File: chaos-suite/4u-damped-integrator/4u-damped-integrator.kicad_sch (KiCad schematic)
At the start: 60 parts, among them J1 BananaJack_PanelMount, J10 BananaJack_PanelMount, J11 BananaJack_PanelMount, J12 I2_IO_Ctrl, J13 I2_IO_Main, J14 I2_Damping_Ctrl, J15 I2_Damping_Main, J16 BananaJack_PanelMount, J2 BananaJack_PanelMount, J3 BananaJack_PanelMount, J4 I1_IO_Ctrl, J5 I1_IO_Main, J6 I1_Damping_Ctrl, J7 I1_Damping_Main, J8 BananaJack_PanelMount, J9 BananaJack_PanelMount, Q1 2N3904, Q2 2N3906, Q3 2N3904, Q4 2N3906, U1 TL074, U2 LM13700

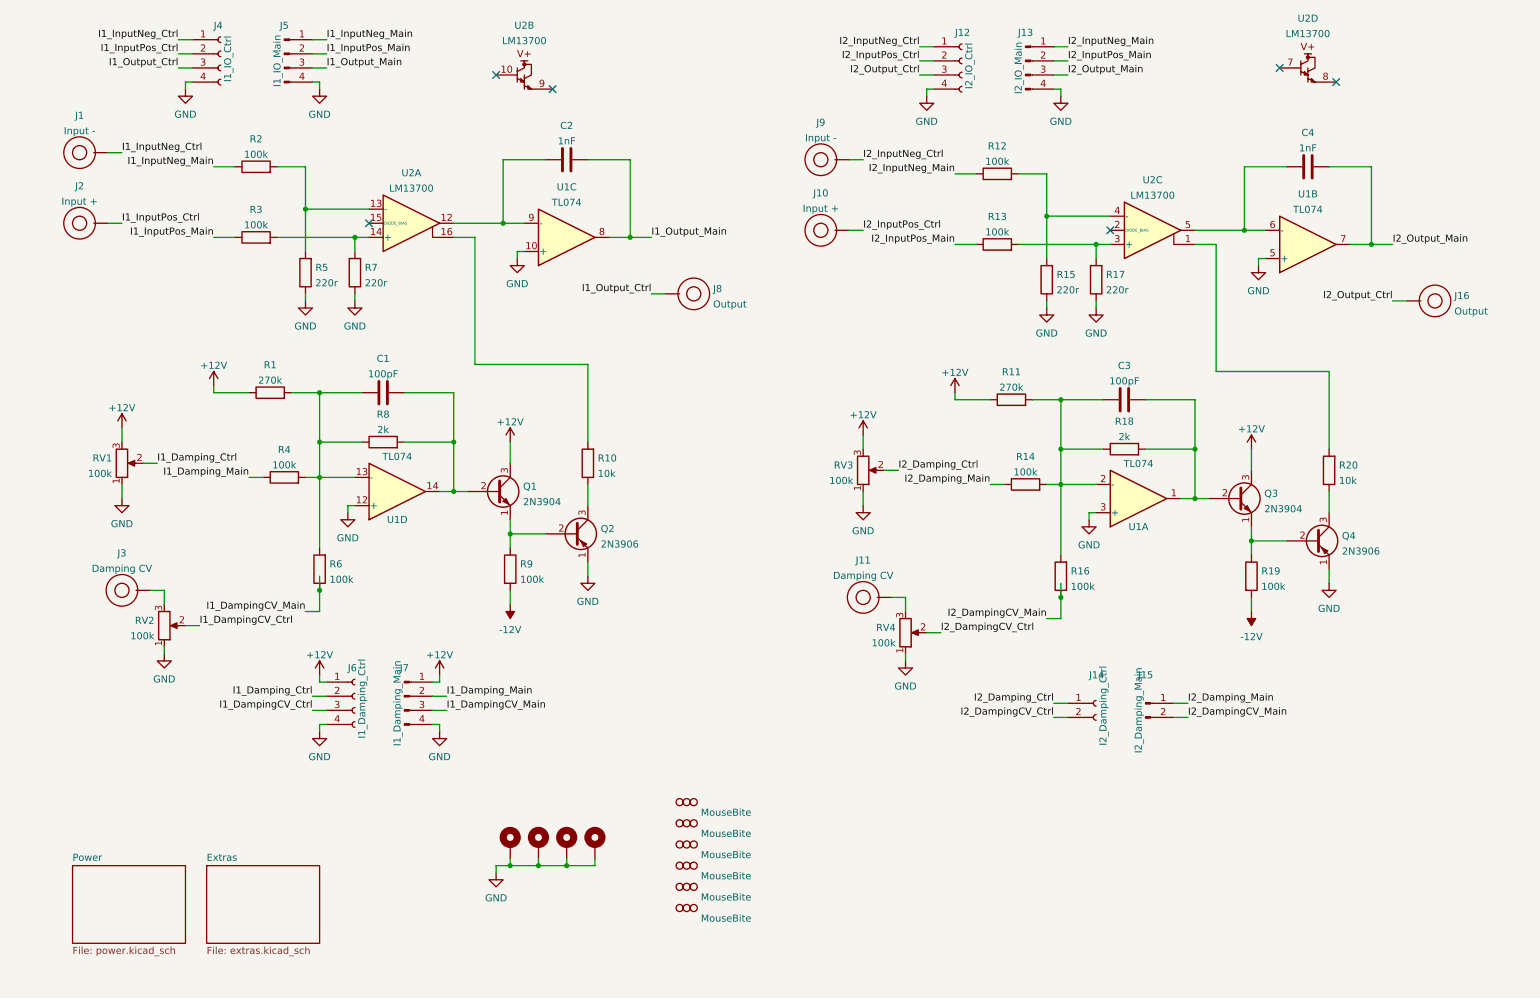
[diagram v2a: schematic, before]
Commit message: Updating damped integrator circuit and layout
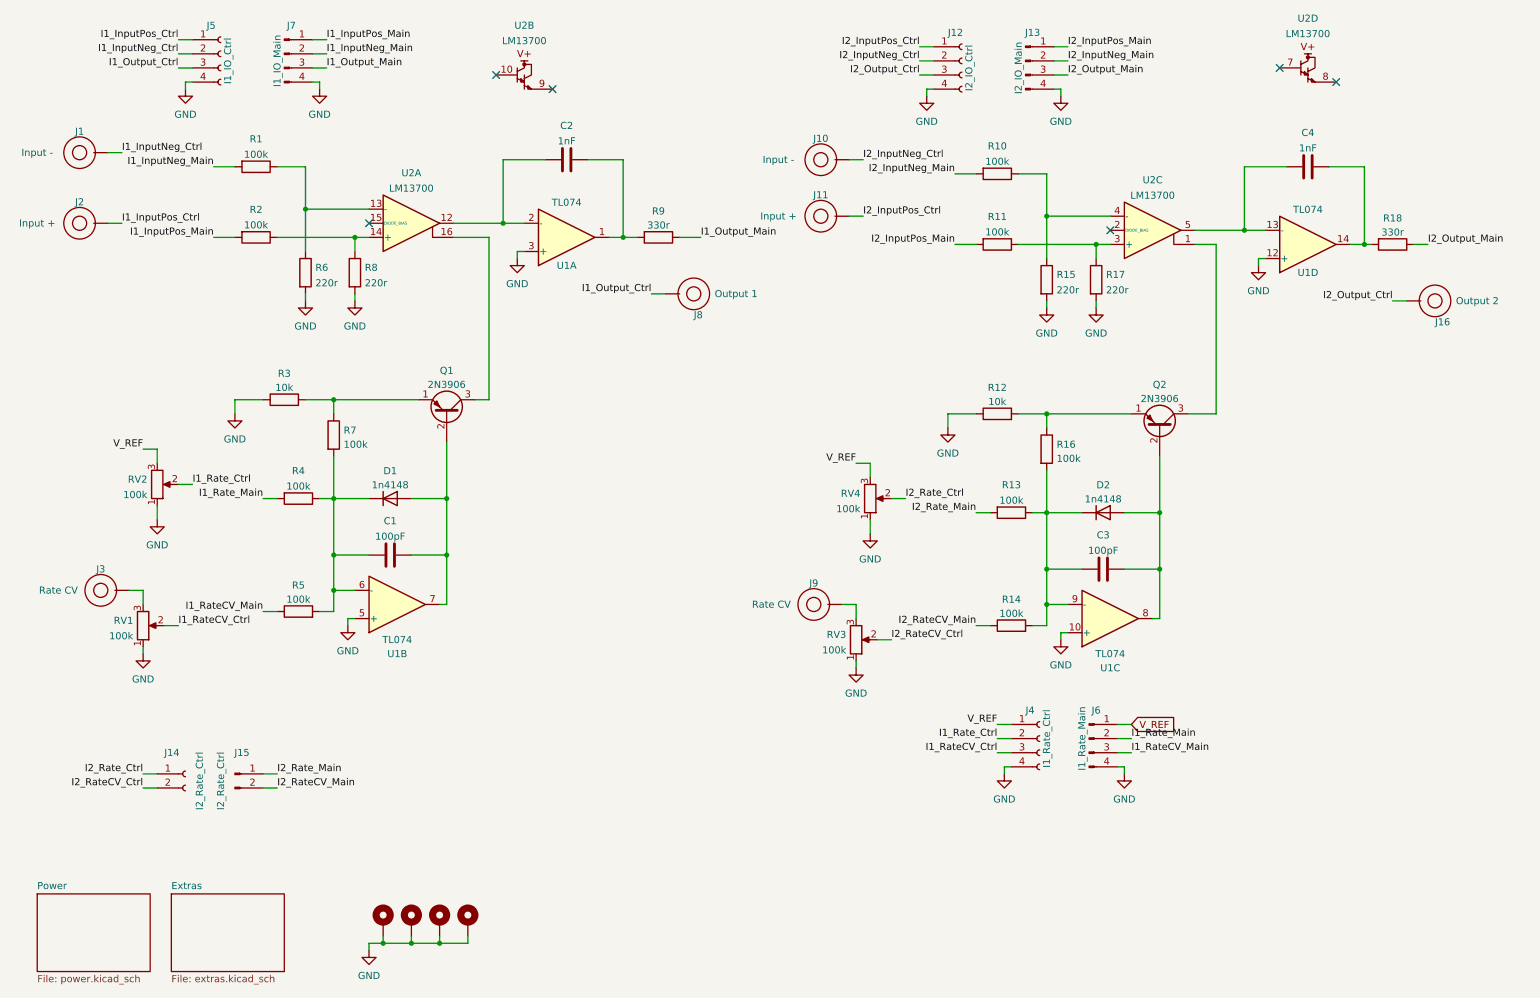
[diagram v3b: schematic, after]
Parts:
- removed H10, H5, H6, H7, H8, H9: MouseBite, Panelization:mouse-bite-2mm-slot, symbol Panelization:MouseBite
- removed J11: BananaJack_PanelMount, Rumblesan_Footprints:BananaJack_THT_JohnsonCinch_108-09, symbol BananaJacks:BananaJack_PanelMount
- removed Q1, Q3: 2N3904, Package_TO_SOT_THT:TO-92_Inline_Wide, symbol Transistor_BJT:2N3904
- removed Q4: 2N3906, Package_TO_SOT_THT:TO-92_Inline_Wide, symbol Transistor_BJT:2N3906
- removed R1, R11: 270k, Rumblesan_Footprints:Resistor_THT_L6.3mm_D2.5mm_P10.16mm_Horizontal, symbol Device:R
- removed R14, R16, R19, R9: 100k, Rumblesan_Footprints:Resistor_THT_L6.3mm_D2.5mm_P10.16mm_Horizontal, symbol Device:R
- removed R18, R8: 2k, Rumblesan_Footprints:Resistor_THT_L6.3mm_D2.5mm_P10.16mm_Horizontal, symbol Device:R
- removed R20: 10k, Rumblesan_Footprints:Resistor_THT_L6.3mm_D2.5mm_P10.16mm_Horizontal, symbol Device:R
- added D1, D2: 1n4148, rumblesan-standard-parts:D_DO-35_SOD27_P7.62mm_Horizontal, symbol Device:D
- added J9: Banana Socket PanelMount, rumblesan-standard-parts:BananaJack_THT_JohnsonCinch_108-09, symbol BananaJacks:Banana Socket PanelMount
- added Q2: 2N3906, Package_TO_SOT_THT:TO-92_Inline_Wide, symbol Transistor_BJT:2N3906
- added R12, R3: 10k, rumblesan-standard-parts:R_Axial_DIN0207_L6.3mm_D2.5mm_P10.16mm_Horizontal, symbol rumblesan-standard-parts:R
- added R13, R14, R16: 100k, rumblesan-standard-parts:R_Axial_DIN0207_L6.3mm_D2.5mm_P10.16mm_Horizontal, symbol rumblesan-standard-parts:R
- added R18, R9: 330r, rumblesan-standard-parts:R_Axial_DIN0207_L6.3mm_D2.5mm_P10.16mm_Horizontal, symbol rumblesan-standard-parts:R
- C1, C2, C3, C4: footprint Rumblesan_Footprints:C_Rect_L7.0mm_W3.5mm_P5.00mm -> rumblesan-standard-parts:C_Rect_L7.0mm_W3.5mm_P5.00mm
- H1, H2, H3, H4: footprint MountingHole:MountingHole_3.2mm_M3_DIN965_Pad -> rumblesan-standard-parts:MountingHole_3.2mm_M3_DIN965_Pad
- J1: value BananaJack_PanelMount -> Banana Socket PanelMount; footprint Rumblesan_Footprints:BananaJack_THT_JohnsonCinch_108-09 -> rumblesan-standard-parts:BananaJack_THT_JohnsonCinch_108-09; symbol BananaJacks:BananaJack_PanelMount -> BananaJacks:Banana Socket PanelMount; Name (none) -> Input -; Note Input - -> (none)
- J10: renamed from J9; value BananaJack_PanelMount -> Banana Socket PanelMount; footprint Rumblesan_Footprints:BananaJack_THT_JohnsonCinch_108-09 -> rumblesan-standard-parts:BananaJack_THT_JohnsonCinch_108-09; symbol BananaJacks:BananaJack_PanelMount -> BananaJacks:Banana Socket PanelMount; Name (none) -> Input -; Note Input - -> (none)
- J11: renamed from J10; value BananaJack_PanelMount -> Banana Socket PanelMount; footprint Rumblesan_Footprints:BananaJack_THT_JohnsonCinch_108-09 -> rumblesan-standard-parts:BananaJack_THT_JohnsonCinch_108-09; symbol BananaJacks:BananaJack_PanelMount -> BananaJacks:Banana Socket PanelMount; Name (none) -> Input +; Note Input + -> (none)
- J12: value I2_IO_Ctrl -> Conn_01x04_Female; Name (none) -> I2_IO_Ctrl
- J13: value I2_IO_Main -> Conn_01x04_Male; Name (none) -> I2_IO_Main
- J14: value I2_Damping_Ctrl -> Conn_01x02_Female; Name (none) -> I2_Rate_Ctrl
- J15: value I2_Damping_Main -> Conn_01x02_Male; Name (none) -> I2_Rate_Ctrl
- J16: value BananaJack_PanelMount -> Banana Socket PanelMount; footprint Rumblesan_Footprints:BananaJack_THT_JohnsonCinch_108-09 -> rumblesan-standard-parts:BananaJack_THT_JohnsonCinch_108-09; symbol BananaJacks:BananaJack_PanelMount -> BananaJacks:Banana Socket PanelMount; Name (none) -> Output 2; Note Output -> (none)
- J2: value BananaJack_PanelMount -> Banana Socket PanelMount; footprint Rumblesan_Footprints:BananaJack_THT_JohnsonCinch_108-09 -> rumblesan-standard-parts:BananaJack_THT_JohnsonCinch_108-09; symbol BananaJacks:BananaJack_PanelMount -> BananaJacks:Banana Socket PanelMount; Name (none) -> Input +; Note Input + -> (none)
- J3: value BananaJack_PanelMount -> Banana Socket PanelMount; footprint Rumblesan_Footprints:BananaJack_THT_JohnsonCinch_108-09 -> rumblesan-standard-parts:BananaJack_THT_JohnsonCinch_108-09; symbol BananaJacks:BananaJack_PanelMount -> BananaJacks:Banana Socket PanelMount; Name (none) -> Rate CV; Note Damping CV -> (none)
- J4: renamed from J6; value I1_Damping_Ctrl -> Conn_01x04_Female; Name (none) -> I1_Rate_Ctrl
- J5: renamed from J4; value I1_IO_Ctrl -> Conn_01x04_Female; Name (none) -> I1_IO_Ctrl
- J6: renamed from J7; value I1_Damping_Main -> Conn_01x04_Male; Name (none) -> I1_Rate_Main
- J7: renamed from J5; value I1_IO_Main -> Conn_01x04_Male; Name (none) -> I1_IO_Main
- J8: value BananaJack_PanelMount -> Banana Socket PanelMount; footprint Rumblesan_Footprints:BananaJack_THT_JohnsonCinch_108-09 -> rumblesan-standard-parts:BananaJack_THT_JohnsonCinch_108-09; symbol BananaJacks:BananaJack_PanelMount -> BananaJacks:Banana Socket PanelMount; Name (none) -> Output 1; Note Output -> (none)
- R1: renamed from R2; footprint Rumblesan_Footprints:Resistor_THT_L6.3mm_D2.5mm_P10.16mm_Horizontal -> rumblesan-standard-parts:R_Axial_DIN0207_L6.3mm_D2.5mm_P10.16mm_Horizontal; symbol Device:R -> rumblesan-standard-parts:R; Power (none) -> 0.5W; Spec (none) -> metal film; Tolerance (none) -> 1%
- R10: renamed from R12; footprint Rumblesan_Footprints:Resistor_THT_L6.3mm_D2.5mm_P10.16mm_Horizontal -> rumblesan-standard-parts:R_Axial_DIN0207_L6.3mm_D2.5mm_P10.16mm_Horizontal; symbol Device:R -> rumblesan-standard-parts:R; Power (none) -> 0.5W; Spec (none) -> metal film; Tolerance (none) -> 1%
- R11: renamed from R13; footprint Rumblesan_Footprints:Resistor_THT_L6.3mm_D2.5mm_P10.16mm_Horizontal -> rumblesan-standard-parts:R_Axial_DIN0207_L6.3mm_D2.5mm_P10.16mm_Horizontal; symbol Device:R -> rumblesan-standard-parts:R; Power (none) -> 0.5W; Spec (none) -> metal film; Tolerance (none) -> 1%
- R15, R17, R4: footprint Rumblesan_Footprints:Resistor_THT_L6.3mm_D2.5mm_P10.16mm_Horizontal -> rumblesan-standard-parts:R_Axial_DIN0207_L6.3mm_D2.5mm_P10.16mm_Horizontal; symbol Device:R -> rumblesan-standard-parts:R; Power (none) -> 0.5W; Spec (none) -> metal film; Tolerance (none) -> 1%
- R2: renamed from R3; footprint Rumblesan_Footprints:Resistor_THT_L6.3mm_D2.5mm_P10.16mm_Horizontal -> rumblesan-standard-parts:R_Axial_DIN0207_L6.3mm_D2.5mm_P10.16mm_Horizontal; symbol Device:R -> rumblesan-standard-parts:R; Power (none) -> 0.5W; Spec (none) -> metal film; Tolerance (none) -> 1%
- R5: renamed from R6; footprint Rumblesan_Footprints:Resistor_THT_L6.3mm_D2.5mm_P10.16mm_Horizontal -> rumblesan-standard-parts:R_Axial_DIN0207_L6.3mm_D2.5mm_P10.16mm_Horizontal; symbol Device:R -> rumblesan-standard-parts:R; Power (none) -> 0.5W; Spec (none) -> metal film; Tolerance (none) -> 1%
- R6: renamed from R5; footprint Rumblesan_Footprints:Resistor_THT_L6.3mm_D2.5mm_P10.16mm_Horizontal -> rumblesan-standard-parts:R_Axial_DIN0207_L6.3mm_D2.5mm_P10.16mm_Horizontal; symbol Device:R -> rumblesan-standard-parts:R; Power (none) -> 0.5W; Spec (none) -> metal film; Tolerance (none) -> 1%
- R7: renamed from R10; value 10k -> 100k; footprint Rumblesan_Footprints:Resistor_THT_L6.3mm_D2.5mm_P10.16mm_Horizontal -> rumblesan-standard-parts:R_Axial_DIN0207_L6.3mm_D2.5mm_P10.16mm_Horizontal; symbol Device:R -> rumblesan-standard-parts:R; Power (none) -> 0.5W; Spec (none) -> metal film; Tolerance (none) -> 1%
- R8: renamed from R7; footprint Rumblesan_Footprints:Resistor_THT_L6.3mm_D2.5mm_P10.16mm_Horizontal -> rumblesan-standard-parts:R_Axial_DIN0207_L6.3mm_D2.5mm_P10.16mm_Horizontal; symbol Device:R -> rumblesan-standard-parts:R; Power (none) -> 0.5W; Spec (none) -> metal film; Tolerance (none) -> 1%
- RV1: renamed from RV2; footprint Rumblesan_Footprints:Potentiometer_Alpha_RD901F-40-00D_Single_Vertical_CircularHoles -> rumblesan-standard-parts:Potentiometer_Alpha_RD901F-40-00D_Single_Vertical
- RV2: renamed from RV1; footprint Rumblesan_Footprints:Potentiometer_Alpha_RD901F-40-00D_Single_Vertical_CircularHoles -> rumblesan-standard-parts:Potentiometer_Alpha_RD901F-40-00D_Single_Vertical
- RV3, RV4: footprint Rumblesan_Footprints:Potentiometer_Alpha_RD901F-40-00D_Single_Vertical_CircularHoles -> rumblesan-standard-parts:Potentiometer_Alpha_RD901F-40-00D_Single_Vertical
- U1: footprint Rumblesan_Footprints:DIP-14_W7.62mm_Socket -> rumblesan-standard-parts:DIP-14_W7.62mm_Socket
- U2: footprint Rumblesan_Footprints:DIP-16_W7.62mm_Socket -> rumblesan-standard-parts:DIP-16_W7.62mm_Socket
- renumbered Q2 to Q1
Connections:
- net GND: now also R15.2, R17.2, R6.2, R8.2, R12.1, R3.1; no longer Q1.1 (E), R15.1, R17.1, R6.1, R8.1
- net I1_InputNeg_Ctrl: now also J5.2 (Pin_2); no longer J5.1 (Pin_1)
- net I1_InputNeg_Main: now also J7.2 (Pin_2), R1.2; no longer J7.1 (Pin_1), R1.1
- net I1_InputPos_Ctrl: now also J5.1 (Pin_1); no longer J5.2 (Pin_2)
- net I1_InputPos_Main: now also J7.1 (Pin_1), R2.2; no longer J7.2 (Pin_2), R2.1
- net I1_Output_Main: now also R9.1; no longer C2.2, U1.8
- net I2_InputNeg_Ctrl: now also J12.2 (Pin_2); no longer J12.1 (Pin_1)
- net I2_InputNeg_Main: now also J13.2 (Pin_2), R10.2; no longer J13.1 (Pin_1), R10.1
- net I2_InputPos_Ctrl: now also J12.1 (Pin_1); no longer J12.2 (Pin_2)
- net I2_InputPos_Main: now also J13.1 (Pin_1), R11.2; no longer J13.2 (Pin_2), R11.1
- net I2_Output_Main: now also R18.1; no longer C4.2, U1.7
- net at C2.1, U2.12: now also U1.2 (-); no longer U1.9 (-)
- net at R7.1: now also Q1.1 (E), R3.2; no longer Q1.3 (C)
- net at R7.2: now also C1.1, R4.1, R5.2, U1.6 (-), D1.1 (K); no longer U2.16
- net at C1.2: now also Q1.2 (B), U1.7, D1.2 (A); no longer U1.14
- net at C4.1, U2.5: now also U1.13 (-); no longer U1.6 (-)
- net at U1.1: now also C2.2, R9.2; no longer C3.2
- net at C3.1: now also U1.9 (-), D2.1 (K), R13.1, R14.2, R16.2; no longer U1.2 (-)
- net at U2.1: now also Q2.3 (C)
- net V_REF: now reaches RV4.3
- net V_REF: now also J4.1 (Pin_1), J6.1 (Pin_1), RV2.3
- removed net +12V: J4.1 (Pin_1), J6.1 (Pin_1), RV2.3, RV3.3
- net I1_DampingCV_Ctrl renamed I1_RateCV_Ctrl
- net I1_DampingCV_Main renamed I1_RateCV_Main
- net I1_Damping_Ctrl renamed I1_Rate_Ctrl
- net I1_Damping_Main renamed I1_Rate_Main
- net I1_Rate_Main: now also R4.2; no longer R4.1
- net I2_DampingCV_Ctrl renamed I2_RateCV_Ctrl
- net I2_RateCV_Ctrl: now also RV3.2; no longer RV4.2
- net I2_DampingCV_Main renamed I2_RateCV_Main
- net I2_RateCV_Main: now also R14.1
- net I2_Damping_Ctrl renamed I2_Rate_Ctrl
- net I2_Rate_Ctrl: now also RV4.2; no longer RV3.2
- net I2_Damping_Main renamed I2_Rate_Main
- net I2_Rate_Main: now also R13.2
- new net: C3.2, D2.2 (A), Q2.2 (B), U1.8
- new net: Q2.1 (E), R12.2, R16.1
- new net: R10.1, R15.1, U2.4 (-)
- new net: R11.1, R17.1, U2.3 (+)
- new net: Q1.3 (C), U2.16
- new net: R2.1, R8.1, U2.14 (+)
- new net: J9.1, RV3.3
- new net: C4.2, R18.2, U1.14
- new net: R1.1, R6.1, U2.13 (-)
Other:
- moved on the sheet: C1, J11, J14, J15, J3, J4, J6, Q1, R4, R5, R7, RV1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
